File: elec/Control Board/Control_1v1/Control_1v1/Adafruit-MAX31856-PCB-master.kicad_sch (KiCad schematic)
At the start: 8 parts, among them J10 MCP9600, J8 MCP9600, J9 MCP9600

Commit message: Add sheet with title block.
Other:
- company: (none) -> Public Invention
- title: (none) -> Control Interconnect Board

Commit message: Fix J10 backwards.
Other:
- title: Control Interconnect Board -> Control Interconnect Board OEDCS
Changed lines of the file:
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@@
   (paper "USLedger")
   (title_block
-    (title "Control Interconnect Board")
+    (title "Control Interconnect Board OEDCS")
     (date "2023-10-10")
     (rev "Rev 1.1")
     (company "Public Invention")
-    (comment 1 "Contributor: Lawrence Kinceloe")
+    (comment 1 "GNU Affero General Public License v3.0")
+    (comment 2 "Contributor: Lawrence Kinceloe")
+    (comment 3 "Drawn By: (Forrest) Lee Erickson")
   )
   (junction (at 88.9 34.29) (diameter 0) (color 0 0 0 0)

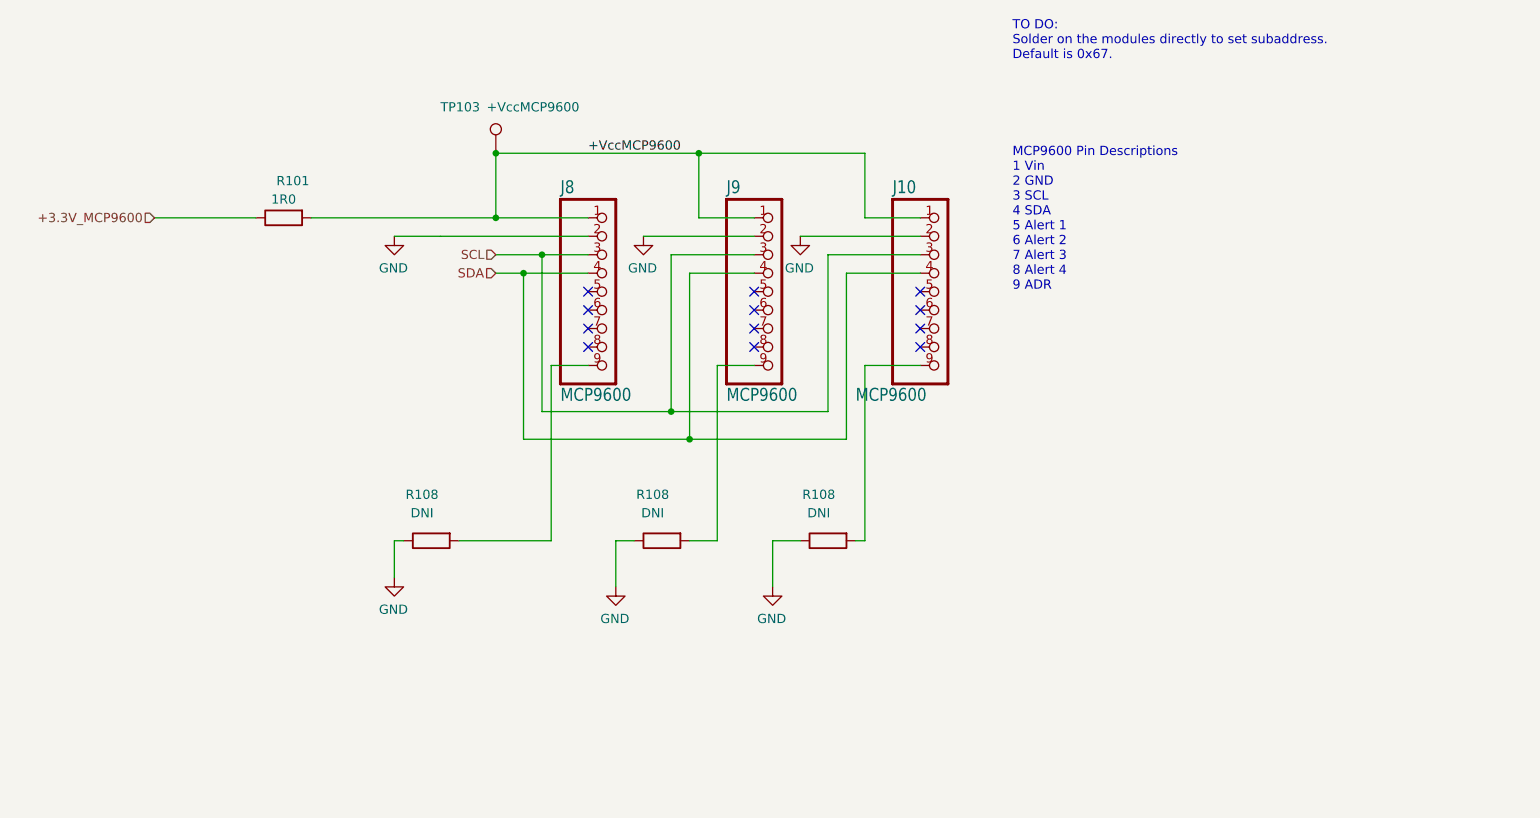
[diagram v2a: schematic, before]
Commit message: Add second power supply connector. Add second and third SSR Driver. Add reset discharge.
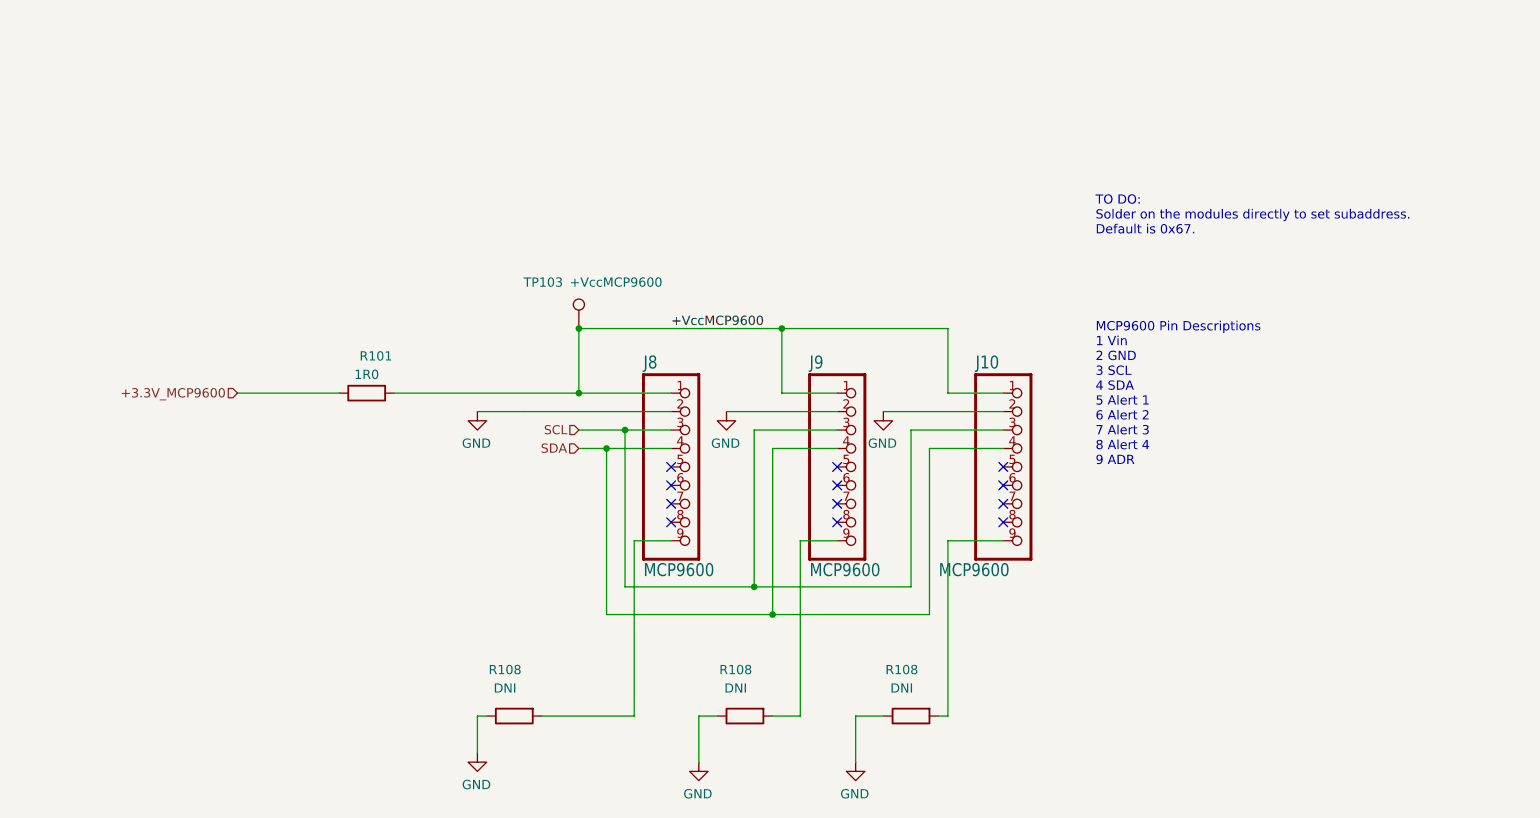
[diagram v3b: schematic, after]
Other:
- moved on the sheet: J10, J8, J9, R101, R108, TP103

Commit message: Add power shutdown button. Add thermocouple ground screw terminals. Isolate SCL from SDA traces. Make first cut BOM.
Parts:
- R101: LongLead (none) -> NO
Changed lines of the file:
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@@
+      (effects (font (size 1.27 1.27)) hide)
+    )
+    (property "LongLead" "NO" (at 71.12 67.31 0)
       (effects (font (size 1.27 1.27)) hide)
     )
